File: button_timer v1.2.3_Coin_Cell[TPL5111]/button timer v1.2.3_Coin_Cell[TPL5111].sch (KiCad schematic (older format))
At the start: 25 parts, among them J1 Conn_01x05_Female, Q1 IRF540N, SW1 SW_Push, SW2 SW_Push, U1 TPS61097A, U3 TPL5111, X1 ESP-12E

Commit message: TO JUPITER :rocket:
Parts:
- Q1: value IRF540N -> mmbt2222
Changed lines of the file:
@@
 P 5900 5550
 F 0 "Q1" H 6104 5596 50  0000 L CNN
-F 1 "IRF540N" H 6104 5505 50  0000 L CNN
+F 1 "mmbt2222" H 6104 5505 50  0000 L CNN
 F 2 "Package_TO_SOT_SMD:SOT-23" H 6150 5475 50  0001 L CIN
 F 3 "http://www.irf.com/product-info/datasheets/data/irf540n.pdf" H 5900 5550 50  0001 L CNN

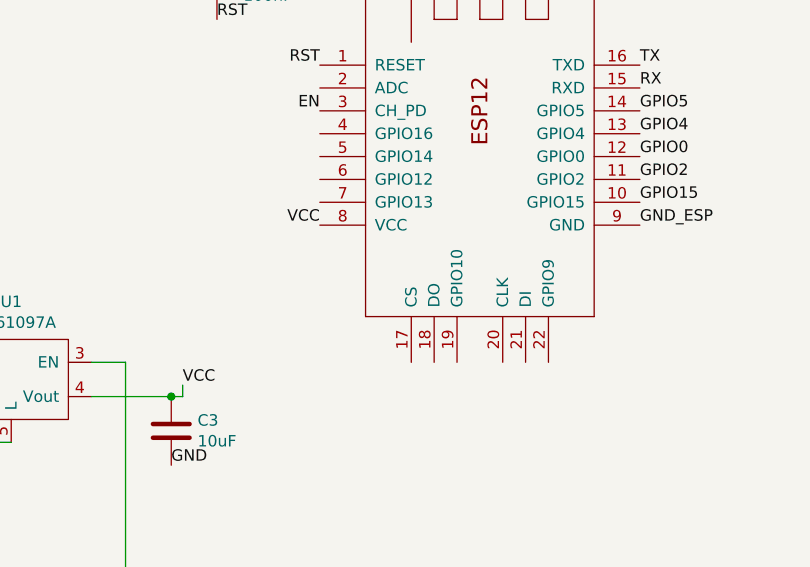
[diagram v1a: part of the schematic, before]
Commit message: cap between esp vcc and ground added
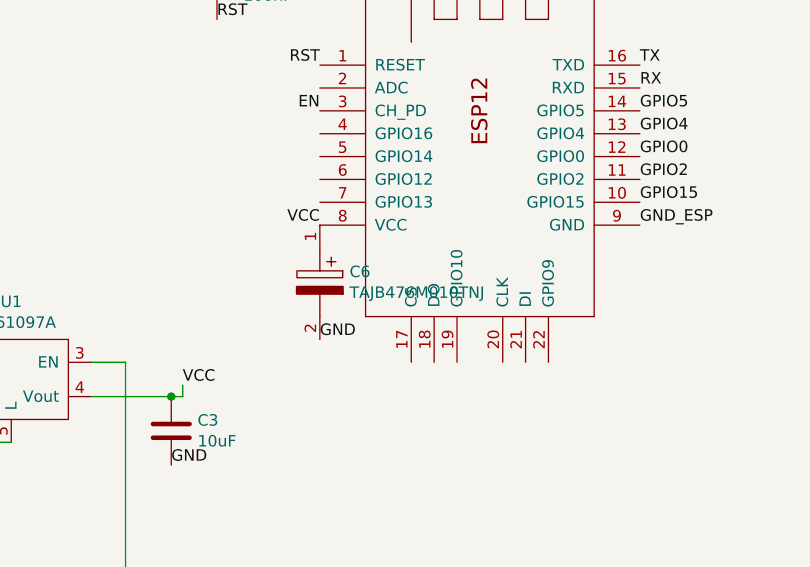
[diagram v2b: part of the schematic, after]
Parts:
- added C6: TAJB476M010TNJ, CAPPM3528X210N, symbol SamacSys_Parts:TAJB476M010TNJ
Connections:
- net GND: now also C6.2
- net VCC: now also C6.1
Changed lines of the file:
@@
 Text Label 6000 5750 0    50   ~ 0
 GND_ESP
+$Comp
+L SamacSys_Parts:TAJB476M010TNJ C6
+U 1 1 60363CFF
+P 5300 3700
+F 0 "C6" V 5504 3830 50  0000 L CNN
+F 1 "TAJB476M010TNJ" V 5595 3830 50  0000 L CNN
+F 2 "CAPPM3528X210N" H 5650 3750 50  0001 L CNN
+F 3 "http://datasheets.avx.com/TAJ.pdf" H 5650 3650 50  0001 L CNN
+F 4 "Tantalum Capacitors - Solid SMD 10volts 47uF 20%" H 5650 3550 50  0001 L CNN "Description"
+F 5 "2.1" H 5650 3450 50  0001 L CNN "Height"
+F 6 "AVX" H 5650 3350 50  0001 L CNN "Manufacturer_Name"
+F 7 "TAJB476M010TNJ" H 5650 3250 50  0001 L CNN "Manufacturer_Part_Number"
+F 8 "581-TAJB476M010TNJ" H 5650 3150 50  0001 L CNN "Mouser Part Number"
+F 9 "https://www.mouser.co.uk/ProductDetail/AVX/TAJB476M010TNJ?qs=pYVYkI7xuRVorIKKgcxm0A%3D%3D" H 5650 3050 50  0001 L CNN "Mouser Price/Stock"
+F 10 "TAJB476M010TNJ" H 5650 2950 50  0001 L CNN "Arrow Part Number"
+F 11 "https://www.arrow.com/en/products/tajb476m010tnj/avx" H 5650 2850 50  0001 L CNN "Arrow Price/Stock"
+	1    5300 3700
+	0    1    1    0
+$EndComp
+Text Label 5300 4200 0    50   ~ 0
+GND
 $EndSCHEMATC
